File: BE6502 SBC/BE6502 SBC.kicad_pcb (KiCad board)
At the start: 2 copper layers, 99.1 x 99.1 mm, 54 parts, among them J1 Expansion, J2 CLOCK_SEL, J3 BARREL_JACK, M1 Mounting, M2 Mounting, M3 Mounting, M4 Mounting, SW1 RESET, SW2 MIDDLE, SW3 UP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

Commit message: Adjusted SBC silkscreen
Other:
- board text added: "$6000 $6001 $6002 $6003"
- board text added: "$FFFA $FFFC $FFFE"
- board text added: "$FFFB $FFFD $FFFF"
- board text added: "1 Mhz"
- board text added: "5v DC"
- board text added: "65C02 CPU"
- board text added: "65C22 VIA"
- board text added: "Clock"
- board text added: "DATA B DATA A DDR B DDR A"
- board text added: "GND"
- board text added: "LCD_EN"
- board text added: "LED_EN"
- board text added: "NMI RST IRQ"
- board text added: "PB0"
- board text added: "PB1"
- board text added: "PB2"
- board text added: "PB3"
- board text added: "PB4"
- board text added: "PB5"
- board text added: "PB6"
- board text added: "PB7"
- board text added: "REGISTERS"
- board text added: "VCC"
- board text added: "VECTORS"
- board text removed: "6502 CPU"
- board text removed: "6522 VIA"

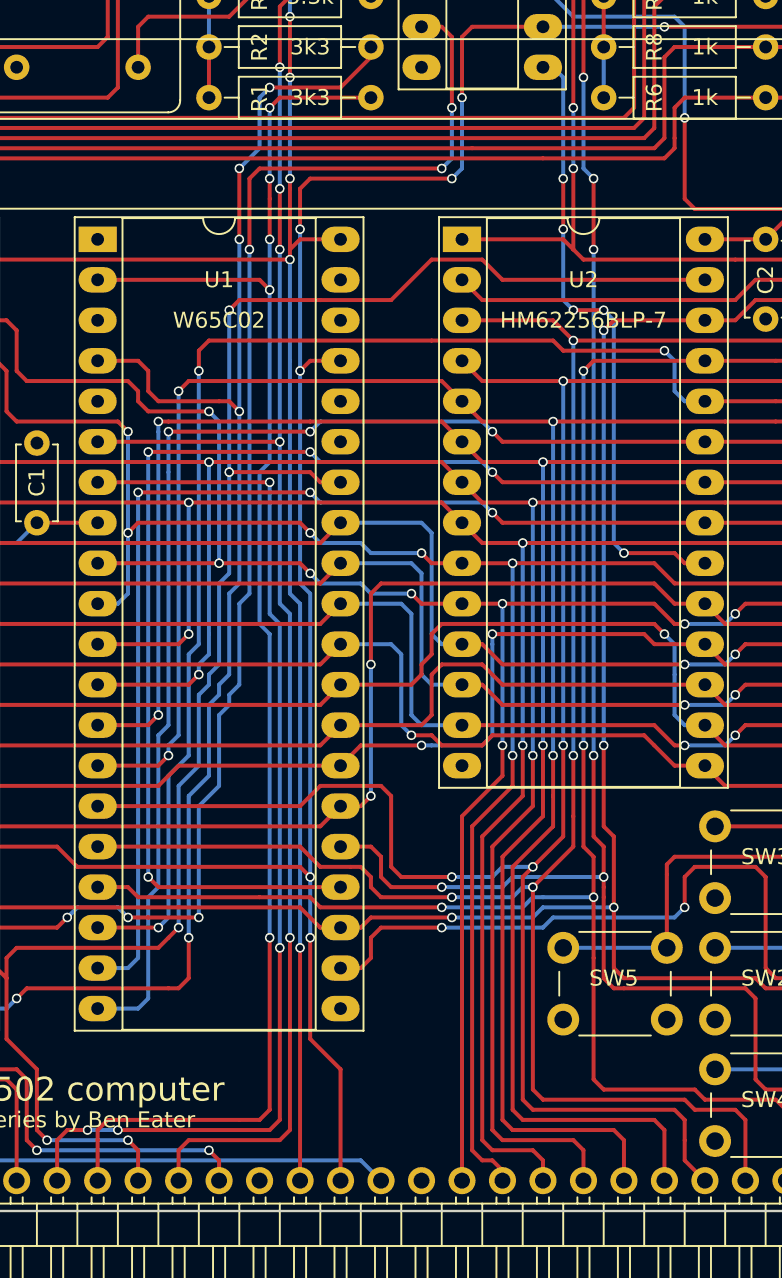
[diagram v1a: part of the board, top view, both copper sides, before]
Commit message: Added BE pin to backplane
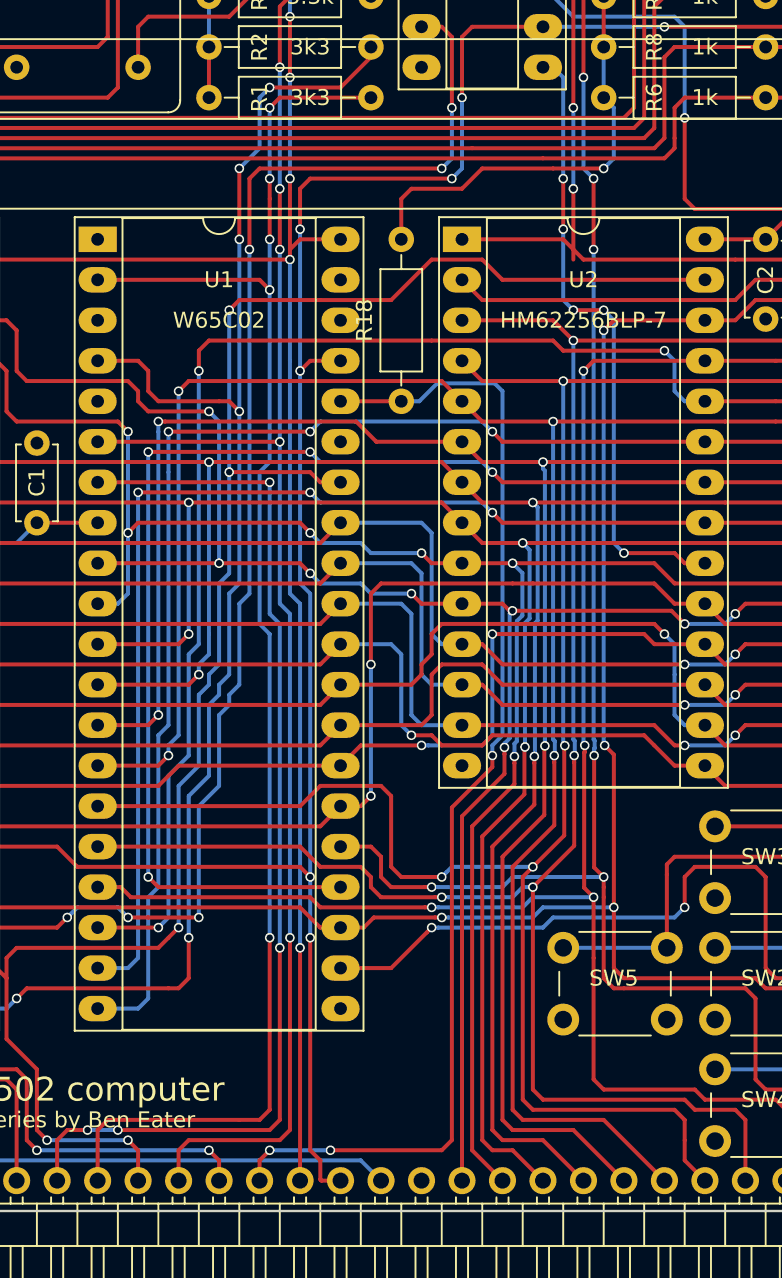
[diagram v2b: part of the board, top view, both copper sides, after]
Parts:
- added R18: 3.3k, Resistors_THT:R_Axial_DIN0207_L6.3mm_D2.5mm_P10.16mm_Horizontal, F.Cu at (156.2, 96.5)
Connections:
- J1 pad 21: (no net) -> /BE
- U1 pad 36: (no net) -> /BE
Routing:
- net /BE: track 0.00 -> 73.0 mm, vias 0 -> 3
- net VCC: track 458.2 -> 479.2 mm, vias 6 -> 7
- net /A5: track 127.8 -> 126.0 mm
- net /A4: track 119.6 -> 118.2 mm
- net /A3: track 124.2 -> 123.4 mm
- net /A12: track 138.8 -> 138.1 mm
- net CLOCK: track 142.5 -> 143.2 mm
- net /A14: track 218.1 -> 218.8 mm

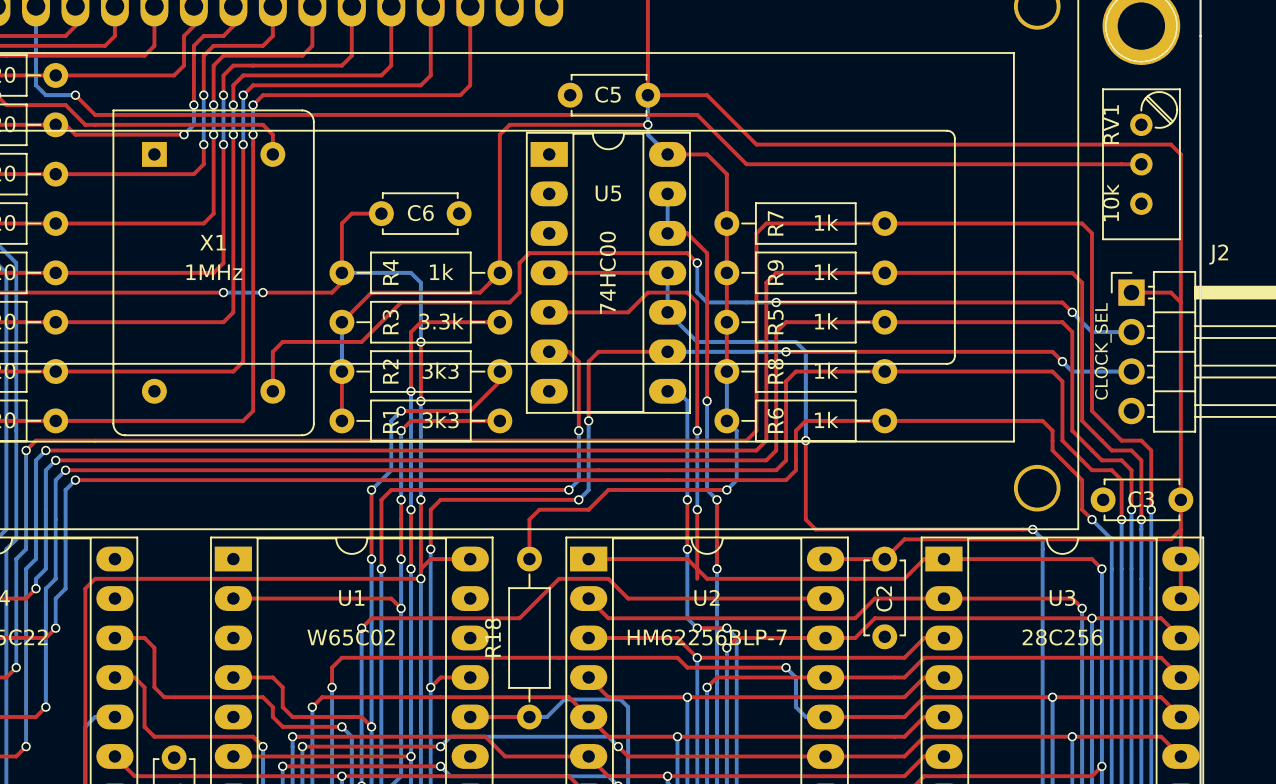
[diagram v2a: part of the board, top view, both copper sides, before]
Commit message: Added current limiting resistor in case more than one clock accidentally activated at the same time
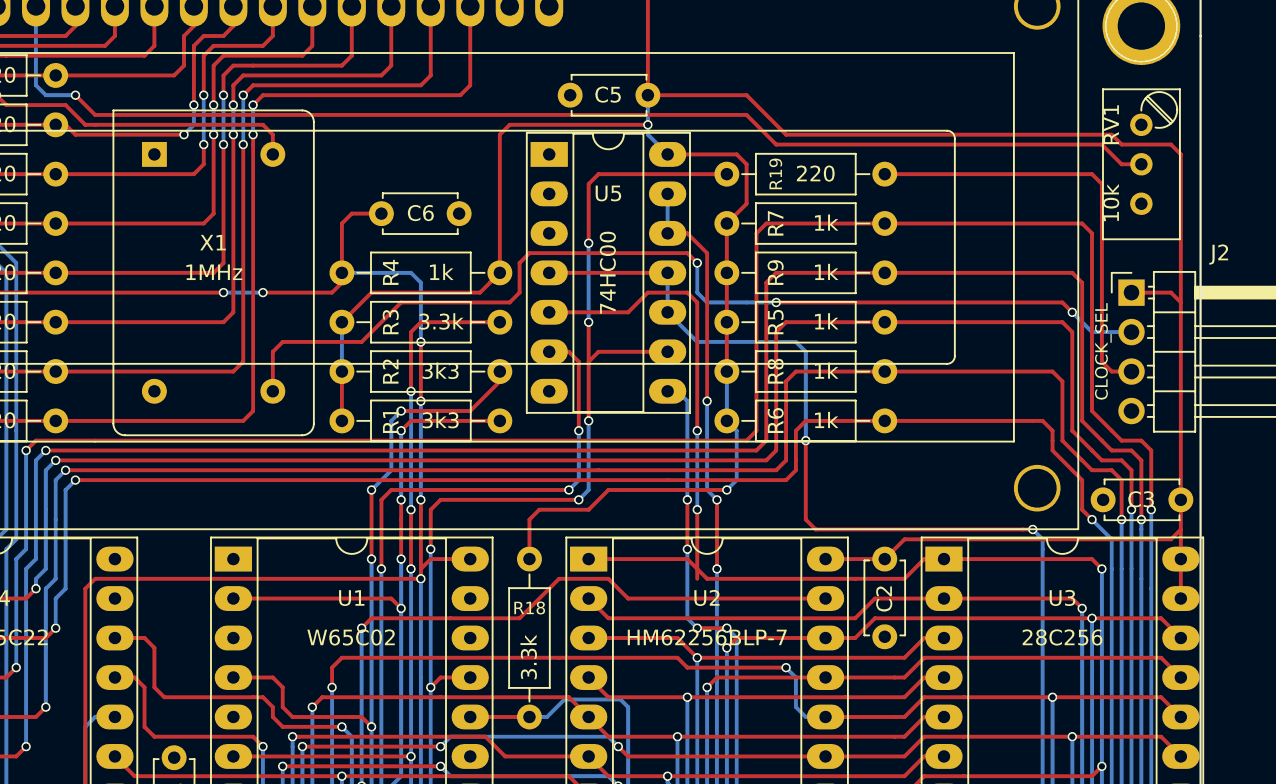
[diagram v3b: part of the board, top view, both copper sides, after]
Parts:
- added R19: 220, Resistors_THT:R_Axial_DIN0207_L6.3mm_D2.5mm_P10.16mm_Horizontal, F.Cu at (168.9, 61.6)
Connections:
- J2 pad 3: CLOCK -> Net-(J2-Pad3)
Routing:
- net Net-(J2-Pad3): track 0.00 -> 27.8 mm
- net CLOCK: track 143.2 -> 133.4 mm
- net VCC: track 479.2 -> 481.4 mm

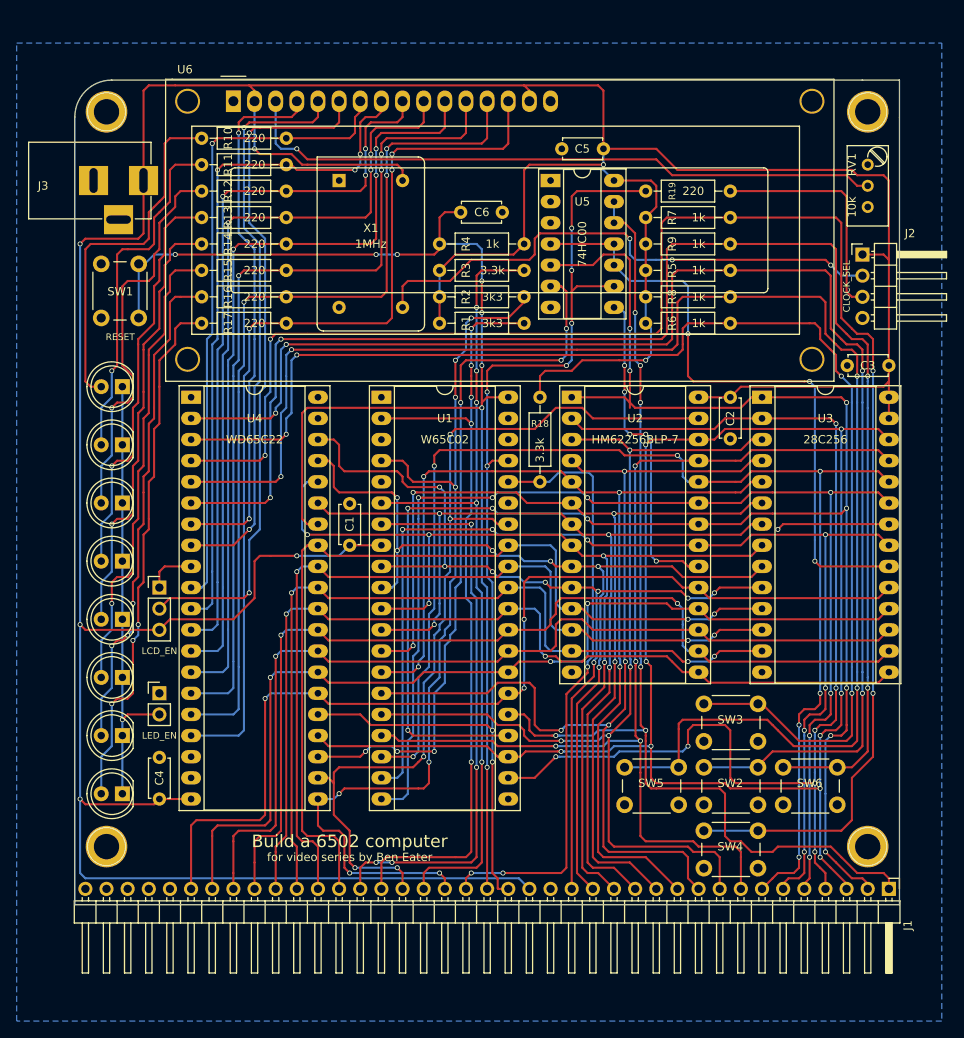
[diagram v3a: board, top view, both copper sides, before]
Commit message: Revised SBC to add reset circuit
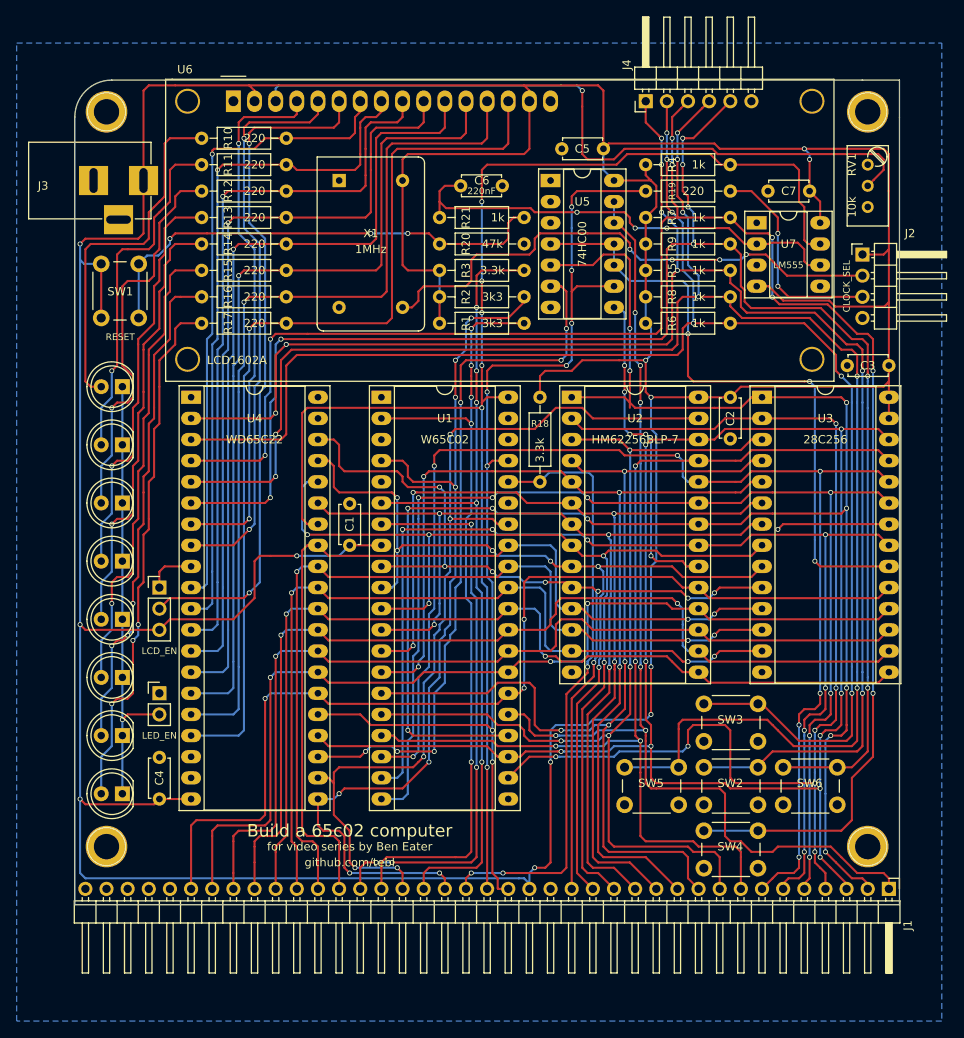
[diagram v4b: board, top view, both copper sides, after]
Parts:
- added C7: 100nF, Capacitors_THT:C_Disc_D4.7mm_W2.5mm_P5.00mm, F.Cu at (188.6, 61.6)
- added J4: Control, Pin_Headers:Pin_Header_Angled_1x06_Pitch2.54mm, F.Cu at (168.9, 50.8)
- added R20: 47k, Resistors_THT:R_Axial_DIN0207_L6.3mm_D2.5mm_P10.16mm_Horizontal, F.Cu at (144.1, 67.9)
- added R21: 1k, Resistors_THT:R_Axial_DIN0207_L6.3mm_D2.5mm_P10.16mm_Horizontal, F.Cu at (144.1, 64.8)
- added U7: LM555, Housings_DIP:DIP-8_W7.62mm_Socket_LongPads, F.Cu at (182.2, 65.4)
- C6: value 100nF -> 220nF
- U6: footprint Displays:WC1602A -> lcd1602a:WC1602A
- moved R4 17.4 mm to (168.9, 58.4), turned to 0 degrees
- moved C6 3.18 mm to (146.7, 61.0)
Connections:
- C6 pad 1: ~RESET -> Net-(C6-Pad1)
- SW1 pad 1: GND -> VCC
- SW1 pad 2: ~RESET -> Net-(R20-Pad1)
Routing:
- net VCC: track 481.4 -> 587.4 mm, vias 7 -> 12
- net Net-(R20-Pad1): track 0.00 -> 57.6 mm, vias 0 -> 3
- net Net-(C6-Pad1): track 0.00 -> 56.2 mm, vias 0 -> 3
- net /PA1: track 158.3 -> 185.5 mm, vias 4 -> 6
- net /PA3: track 186.8 -> 211.0 mm, vias 4 -> 8
- net /PA0: track 172.0 -> 192.1 mm, vias 4 -> 8
- net /PA4: track 181.1 -> 199.7 mm, vias 4 -> 8
- net /PA2: track 199.2 -> 211.7 mm, vias 4 -> 8
- net Net-(RV1-Pad2): track 78.3 -> 87.9 mm
- net ~RESET: track 172.6 -> 177.3 mm, vias 8 -> 6
- net Net-(J2-Pad3): track 27.8 -> 26.0 mm, vias 0 -> 2
- net /~IRQ: track 115.4 -> 113.9 mm
- net /A15: track 129.5 -> 128.9 mm
- net /A2: track 122.9 -> 123.5 mm
- net Net-(J2-Pad2): track 64.8 -> 64.9 mm, vias 3 -> 4
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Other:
- board text added: "1MHZ"
- board text added: "Build a 65c02 computer"
- board text added: "CLK"
- board text added: "LCD1602A"
- board text added: "RESET CIRCUIT"
- board text added: "Revision B"
- board text removed: "1 Mhz"
- board text removed: "BE6502"
- board text removed: "Build a 6502 computer"
- board text removed: "Clock"
- board text removed: "SBC Revision A"
